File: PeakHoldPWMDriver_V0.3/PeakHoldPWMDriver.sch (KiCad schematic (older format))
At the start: 109 parts, among them J1 Screw_Terminal_01x06, J2 Screw_Terminal_01x08, Q1 2N7002, Q10 2N7002, Q11 2N7002, Q12 2N7002, Q13 TSM2309, Q14 IRLL 024N, Q15 TSM2309, Q16 IRLL 024N, Q2 2N7002, Q3 2N7002, Q4 2N7002, Q5 TSM2309, Q6 TSM2309, Q7 IRLL 024N, Q8 IRLL 024N, Q9 2N7002, U1 74LS32, U2 LM2901, U3 74LS74, U4 LTC6992, U5 74LS74, U6 LM78M05, U7 74LS08, U8 74LS08

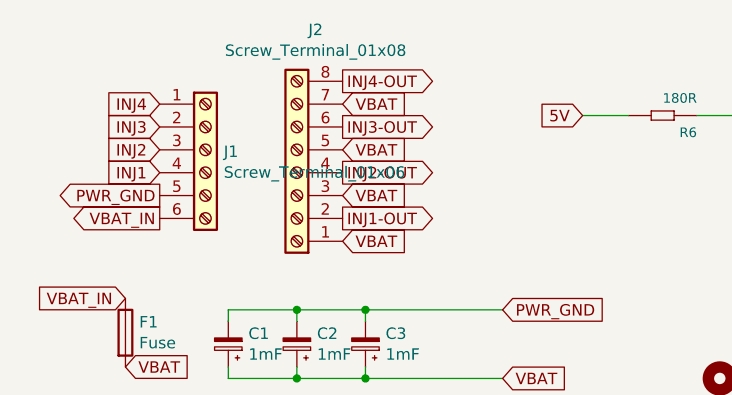
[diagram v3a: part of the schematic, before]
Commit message: Added supplier to BOM list
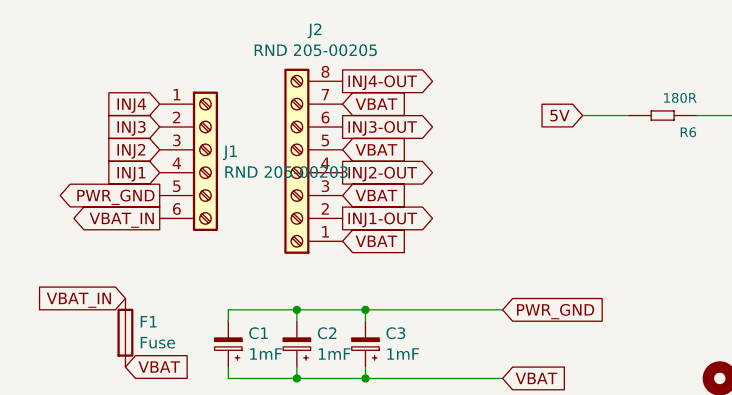
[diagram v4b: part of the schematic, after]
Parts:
- J1: value Screw_Terminal_01x06 -> RND 205-00203
- J2: value Screw_Terminal_01x08 -> RND 205-00205
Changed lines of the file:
@@
 P 1300 1100
 F 0 "J1" H 1380 1092 50  0000 L CNN
-F 1 "Screw_Terminal_01x06" H 1380 1001 50  0000 L CNN
+F 1 "RND 205-00203" H 1380 1001 50  0000 L CNN
 F 2 "Connector_Phoenix_MSTB:PhoenixContact_MSTBA_2,5_6-G-5,08_1x06_P5.08mm_Horizontal" H 1300 1100 50  0001 C CNN
 F 3 "~" H 1300 1100 50  0001 C CNN
@@
 P 1700 1200
 F 0 "J2" H 1618 575 50  0000 C CNN
-F 1 "Screw_Terminal_01x08" H 1618 666 50  0000 C CNN
+F 1 "RND 205-00205" H 1618 666 50  0000 C CNN
 F 2 "Connector_Phoenix_MSTB:PhoenixContact_MSTBA_2,5_8-G-5,08_1x08_P5.08mm_Horizontal" H 1700 1200 50  0001 C CNN
 F 3 "~" H 1700 1200 50  0001 C CNN

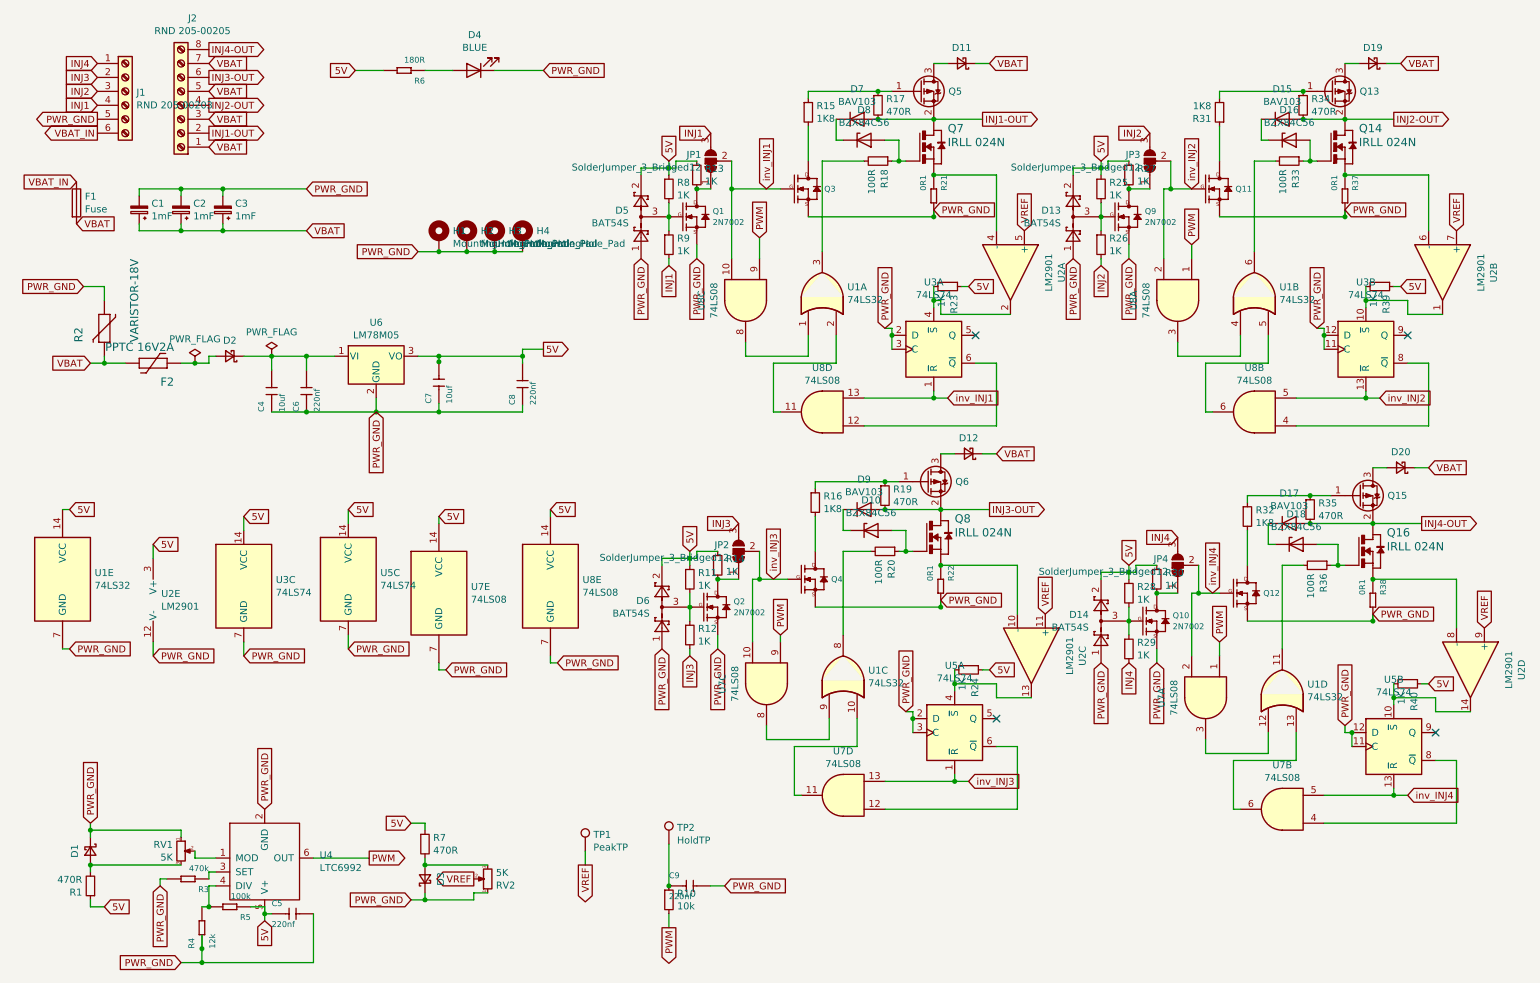
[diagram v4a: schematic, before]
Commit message: Update V0.3 PCB
Updated V0.3 pcb with pulldown resistors when using ECU input. And some Cleanup pcb
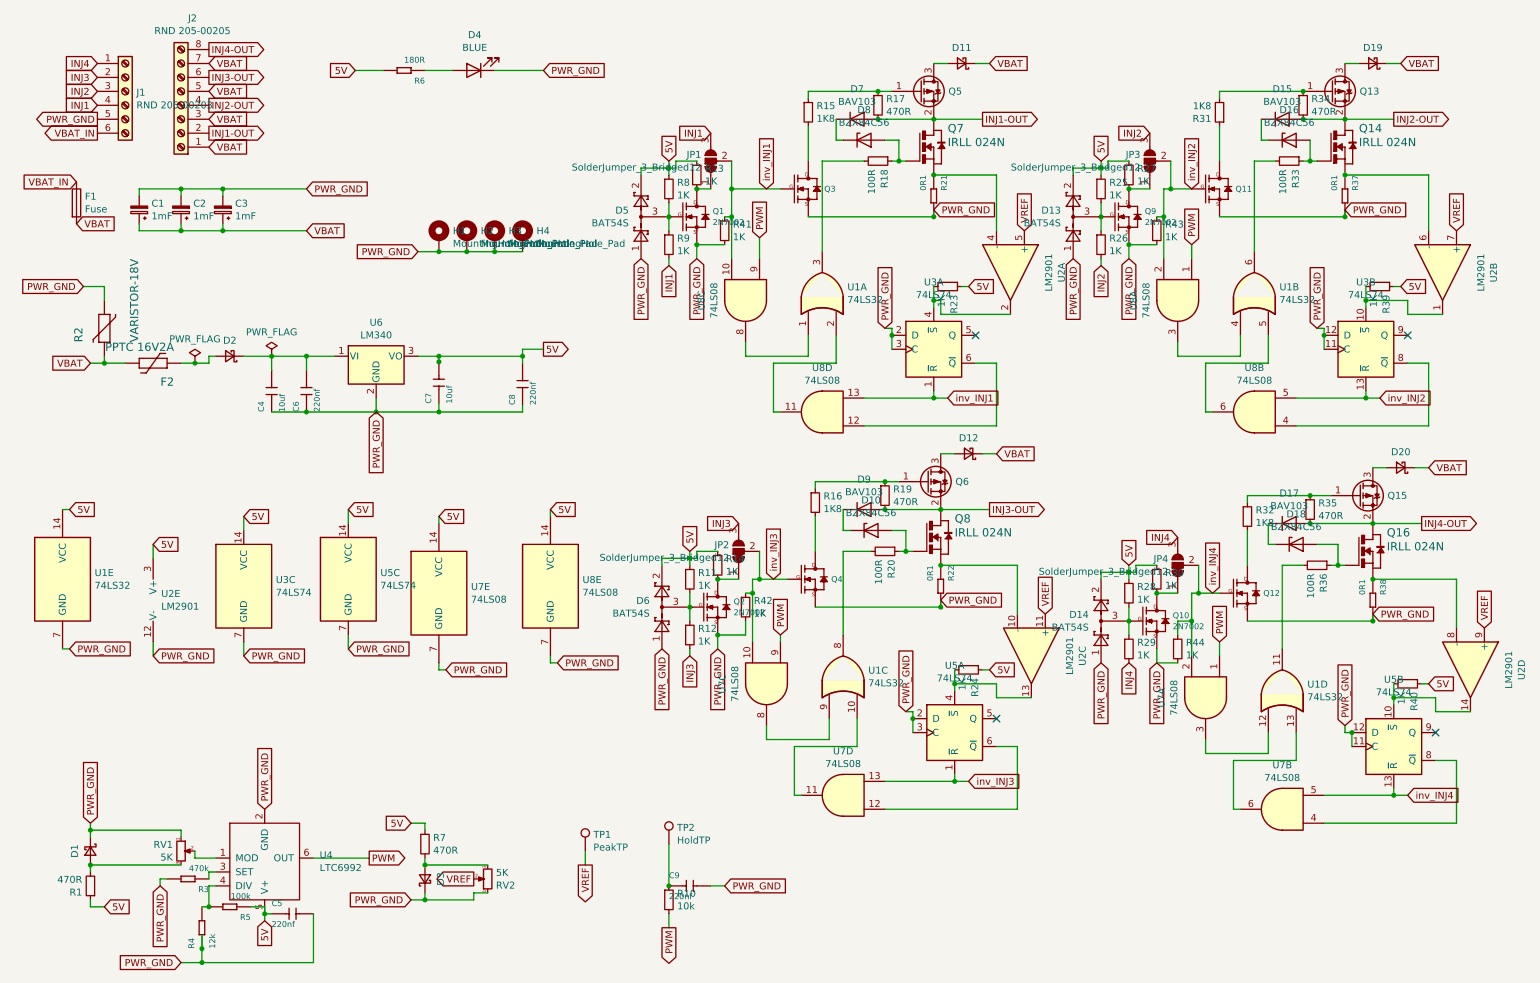
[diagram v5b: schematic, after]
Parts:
- added R41, R42, R43, R44: 1K, Resistor_SMD:R_0603_1608Metric_Pad1.05x0.95mm_HandSolder, symbol Device:R_Small
- U6: value LM78M05 -> LM340
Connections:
- net PWR_GND: now also R41.2, R42.2, R43.2, R44.2
- net inv_INJ1: now also R41.1
- net inv_INJ2: now also R43.1
- net inv_INJ3: now also R42.1
- net inv_INJ4: now also R44.1
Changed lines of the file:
@@
 P 3100 3000
 F 0 "U6" H 3100 3242 50  0000 C CNN
-F 1 "LM78M05" H 3100 3151 50  0000 C CNN
+F 1 "LM340" H 3100 3151 50  0000 C CNN
 F 2 "Package_TO_SOT_SMD:SOT-223-3_TabPin2" H 3100 3225 50  0001 C CIN
 F 3 "http://www.fairchildsemi.com/ds/LM/LM78M05.pdf" H 3100 2950 50  0001 C CNN
@@
 $EndComp
 Wire Wire Line
-	5650 1800 5650 2300
+	5650 1800 5650 2000
 $Comp
 L Device:R_Small R8
@@
 	5200 1650 5200 1700
 Wire Wire Line
-	5800 4600 5800 5050
-Wire Wire Line
-	8950 4700 8950 5150
+	5800 4600 5800 4700
+Wire Wire Line
+	8950 4700 8950 4900
 Wire Wire Line
 	8950 4700 9000 4700
@@
 $EndComp
 Wire Wire Line
-	8750 1800 8750 2300
+	8750 1800 8750 2000
 Text GLabel 8100 2300 3    50   Input ~ 0
 PWR_GND
@@
 	-1   0    0    1
 $EndComp
+$Comp
+L Device:R_Small R42
+U 1 1 5F326DA4
+P 5750 4800
+F 0 "R42" H 5809 4846 50  0000 L CNN
+F 1 "1K" H 5809 4755 50  0000 L CNN
+F 2 "Resistor_SMD:R_0603_1608Metric_Pad1.05x0.95mm_HandSolder" H 5750 4800 50  0001 C CNN
+F 3 "~" H 5750 4800 50  0001 C CNN
+	1    5750 4800
+	1    0    0    -1
+$EndComp
+Wire Wire Line
+	5750 4700 5800 4700
+Connection ~ 5800 4700
+Wire Wire Line
+	5800 4700 5800 5050
+Wire Wire Line
+	5750 4900 5750 5000
+Wire Wire Line
+	5750 5000 5550 5000
+Connection ~ 5550 5000
+$Comp
+L Device:R_Small R44
+U 1 1 5F36C8D9
+P 8850 5100
+F 0 "R44" H 8909 5146 50  0000 L CNN
+F 1 "1K" H 8909 5055 50  0000 L CNN
+F 2 "Resistor_SMD:R_0603_1608Metric_Pad1.05x0.95mm_HandSolder" H 8850 5100 50  0001 C CNN
+F 3 "~" H 8850 5100 50  0001 C CNN
+	1    8850 5100
+	1    0    0    -1
+$EndComp
+Wire Wire Line
+	8850 5000 8850 4900
+Wire Wire Line
+	8850 4900 8950 4900
+Connection ~ 8950 4900
+Wire Wire Line
+	8950 4900 8950 5150
+Wire Wire Line
+	8850 5200 8700 5200
+$Comp
+L Device:R_Small R43
+U 1 1 5F3BB1AD
+P 8700 2100
+F 0 "R43" H 8759 2146 50  0000 L CNN
+F 1 "1K" H 8759 2055 50  0000 L CNN
+F 2 "Resistor_SMD:R_0603_1608Metric_Pad1.05x0.95mm_HandSolder" H 8700 2100 50  0001 C CNN
+F 3 "~" H 8700 2100 50  0001 C CNN
+	1    8700 2100
+	1    0    0    -1
+$EndComp
+Wire Wire Line
+	8700 2000 8750 2000
+Connection ~ 8750 2000
+Wire Wire Line
+	8750 2000 8750 2300
+Wire Wire Line
+	8700 2200 8500 2200
+Connection ~ 8500 2200
+$Comp
+L Device:R_Small R41
+U 1 1 5F3FF496
+P 5600 2100
+F 0 "R41" H 5659 2146 50  0000 L CNN
+F 1 "1K" H 5659 2055 50  0000 L CNN
+F 2 "Resistor_SMD:R_0603_1608Metric_Pad1.05x0.95mm_HandSolder" H 5600 2100 50  0001 C CNN
+F 3 "~" H 5600 2100 50  0001 C CNN
+	1    5600 2100
+	1    0    0    -1
+$EndComp
+Wire Wire Line
+	5600 2200 5400 2200
+Connection ~ 5400 2200
+Wire Wire Line
+	5600 2000 5650 2000
+Connection ~ 5650 2000
+Wire Wire Line
+	5650 2000 5650 2300
 $EndSCHEMATC

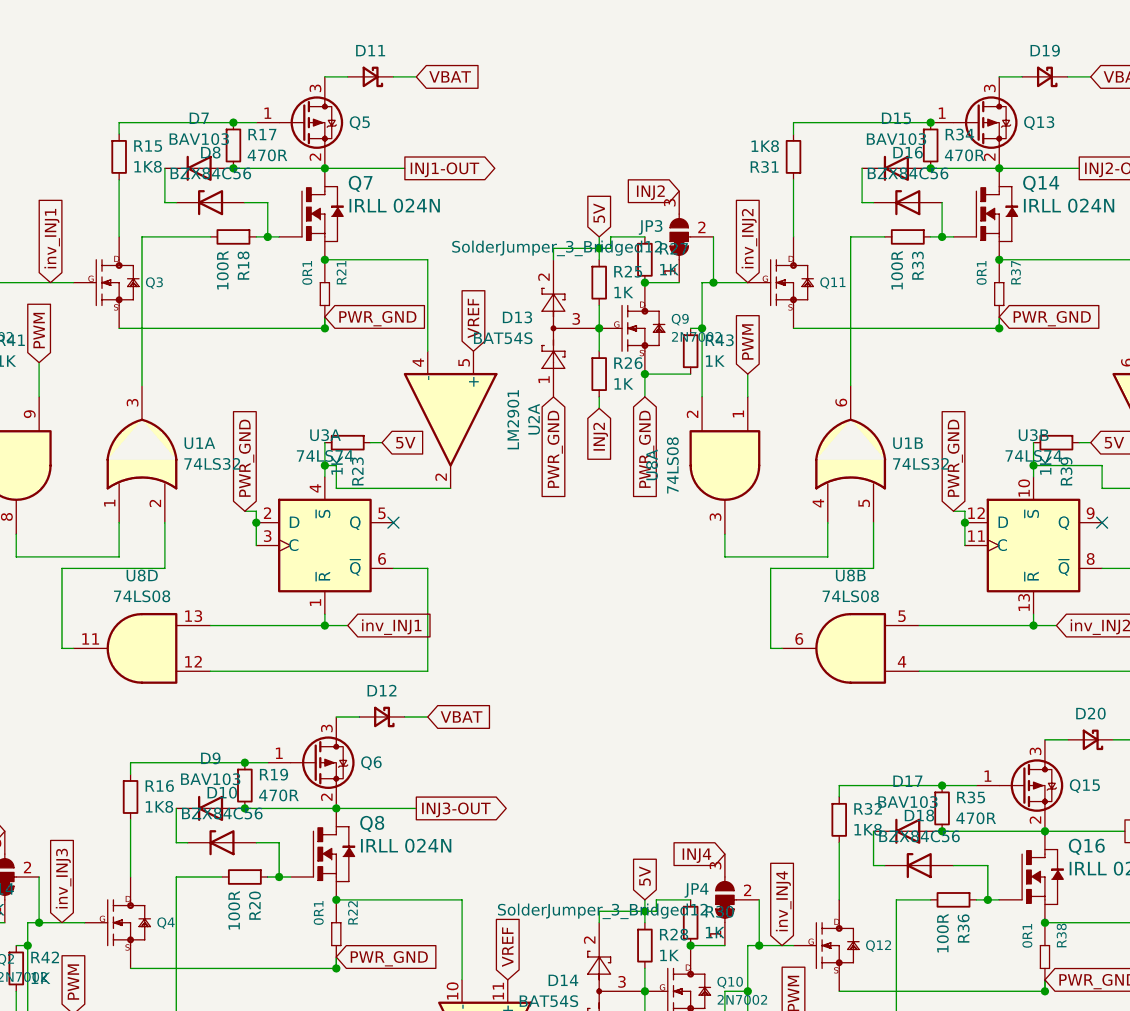
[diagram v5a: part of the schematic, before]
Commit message: Update zener value
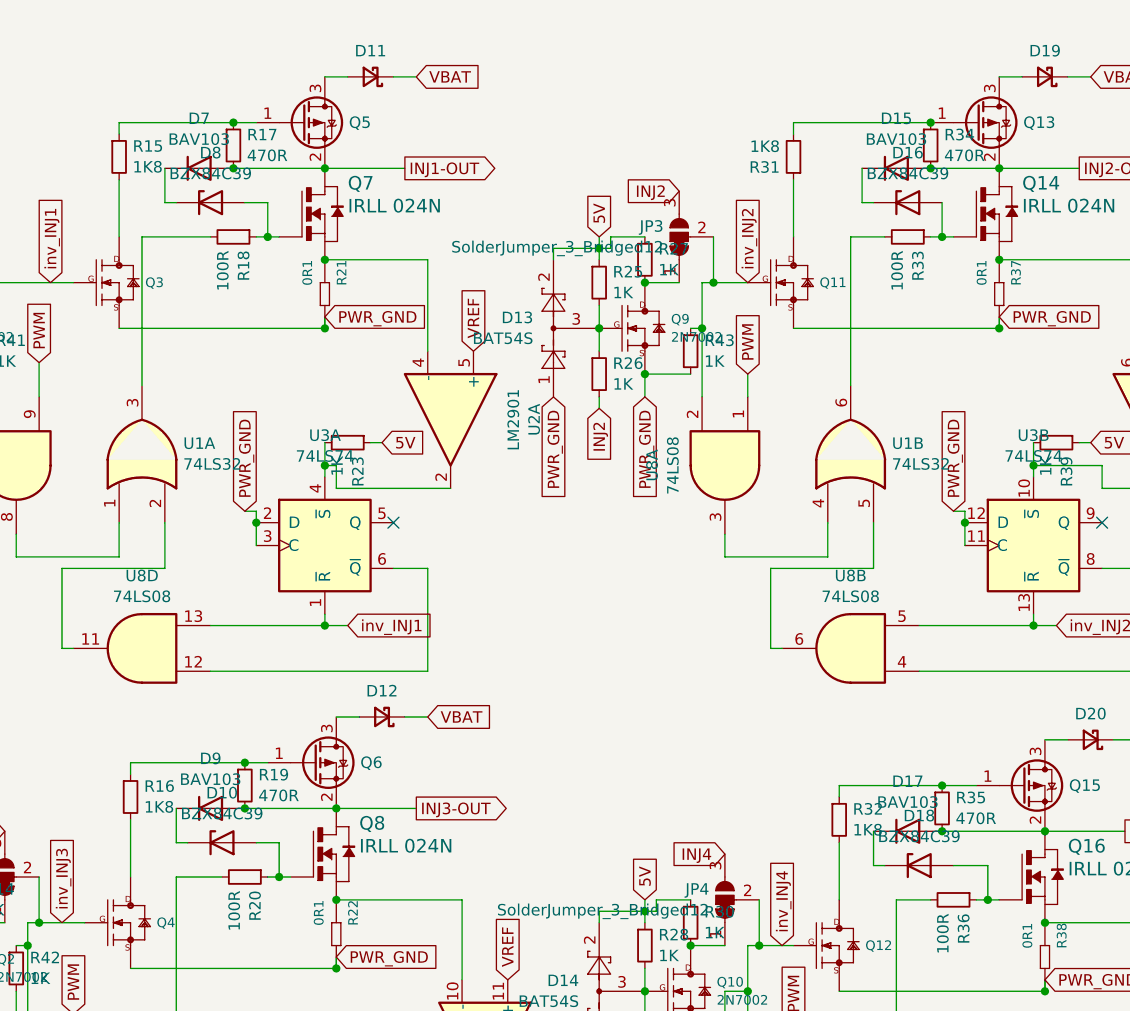
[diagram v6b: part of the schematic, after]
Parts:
- D10, D16, D18, D8: value BZX84C56 -> BZX84C39
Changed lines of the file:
@@
 P 6600 1450
 F 0 "D8" H 6600 1667 50  0000 C CNN
-F 1 "BZX84C56" H 6600 1576 50  0000 C CNN
+F 1 "BZX84C39" H 6600 1576 50  0000 C CNN
 F 2 "Diode_SMD:D_SOT-23_ANK" H 6600 1275 50  0001 C CNN
 F 3 "https://diotec.com/tl_files/diotec/files/pdf/datasheets/bzx84c2v4.pdf" H 6600 1450 50  0001 C CNN
@@
 P 9650 1450
 F 0 "D16" H 9650 1667 50  0000 C CNN
-F 1 "BZX84C56" H 9650 1576 50  0000 C CNN
+F 1 "BZX84C39" H 9650 1576 50  0000 C CNN
 F 2 "Diode_SMD:D_SOT-23_ANK" H 9650 1275 50  0001 C CNN
 F 3 "https://diotec.com/tl_files/diotec/files/pdf/datasheets/bzx84c2v4.pdf" H 9650 1450 50  0001 C CNN
@@
 P 6650 4250
 F 0 "D10" H 6650 4467 50  0000 C CNN
-F 1 "BZX84C56" H 6650 4376 50  0000 C CNN
+F 1 "BZX84C39" H 6650 4376 50  0000 C CNN
 F 2 "Diode_SMD:D_SOT-23_ANK" H 6650 4075 50  0001 C CNN
 F 3 "https://diotec.com/tl_files/diotec/files/pdf/datasheets/bzx84c2v4.pdf" H 6650 4250 50  0001 C CNN
@@
 P 9700 4350
 F 0 "D18" H 9700 4567 50  0000 C CNN
-F 1 "BZX84C56" H 9700 4476 50  0000 C CNN
+F 1 "BZX84C39" H 9700 4476 50  0000 C CNN
 F 2 "Diode_SMD:D_SOT-23_ANK" H 9700 4175 50  0001 C CNN
 F 3 "https://diotec.com/tl_files/diotec/files/pdf/datasheets/bzx84c2v4.pdf" H 9700 4350 50  0001 C CNN
